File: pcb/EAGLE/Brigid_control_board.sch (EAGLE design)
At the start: 33 parts, among them J1 ARDUINO_R3_SHIELD, P1 Molex Mini-Fit Jr., P2 Molex Mini-Fit Jr., P3 Molex Mini-Fit Jr., P4 Molex Mini-Fit Jr., P5 Molex Mini-Fit Jr., P6 Molex Mini-Fit Jr., P7 Molex Mini-Fit Jr., Q1 T460, Q2 T460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

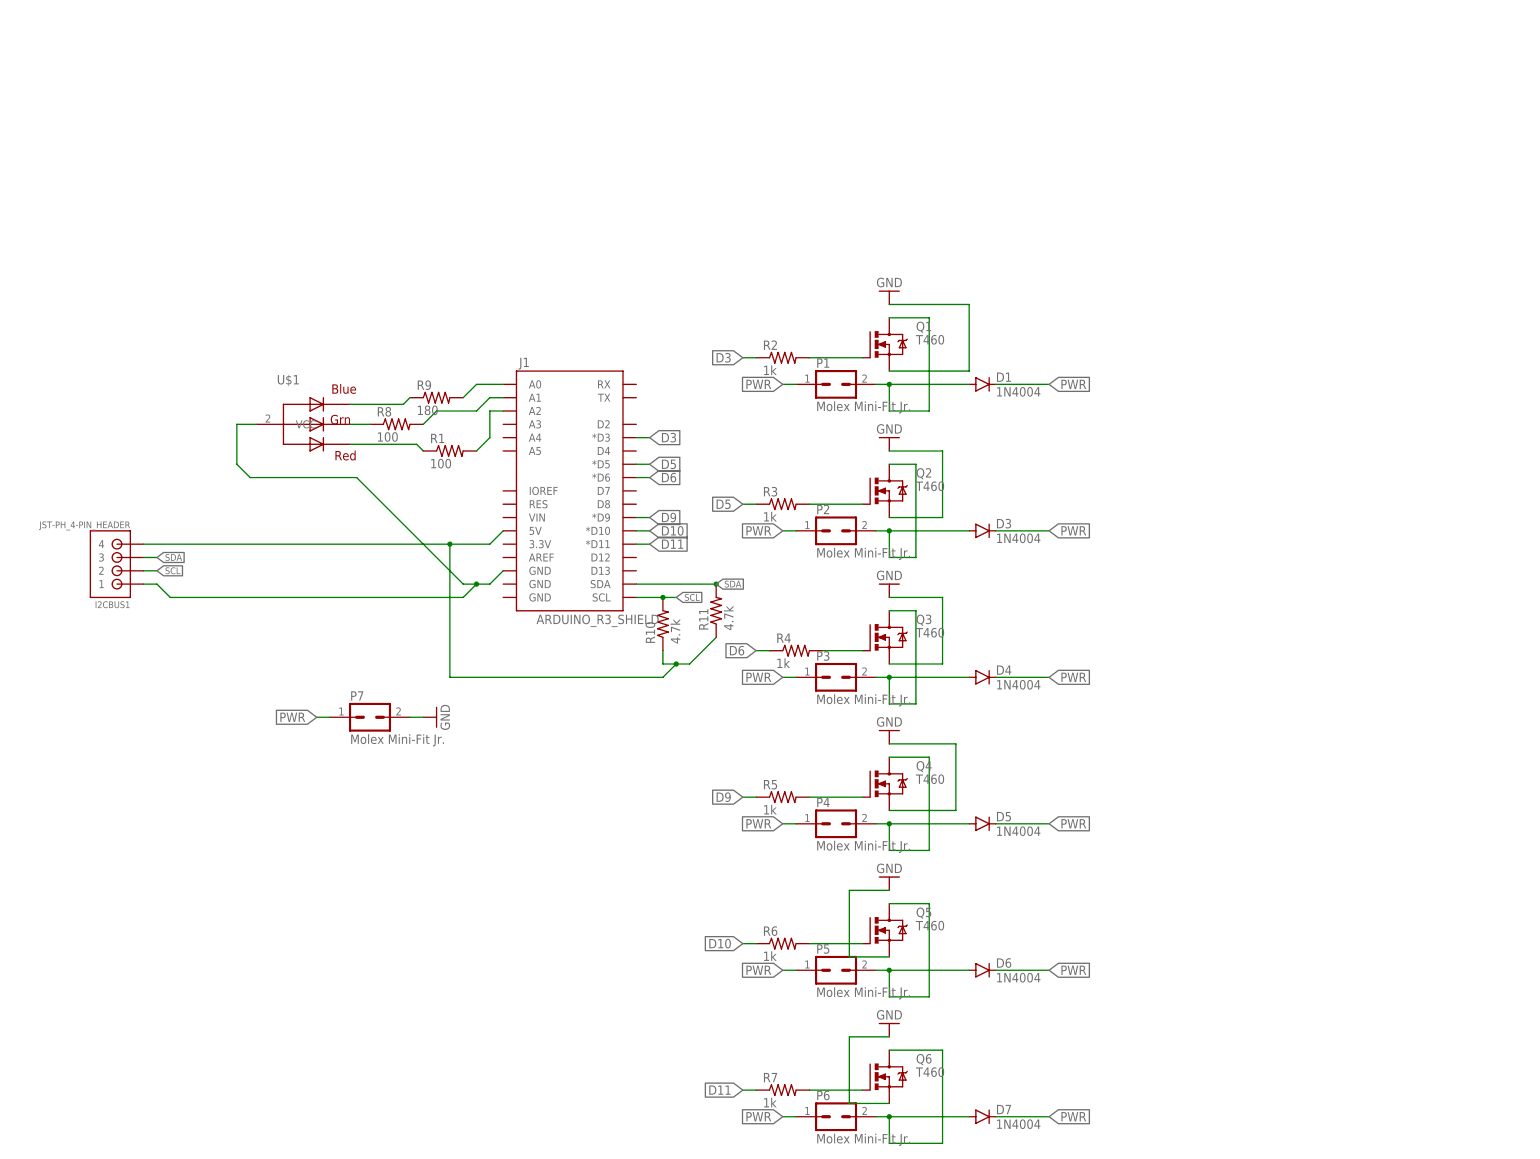
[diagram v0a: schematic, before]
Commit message: added firmware for DC_Motors
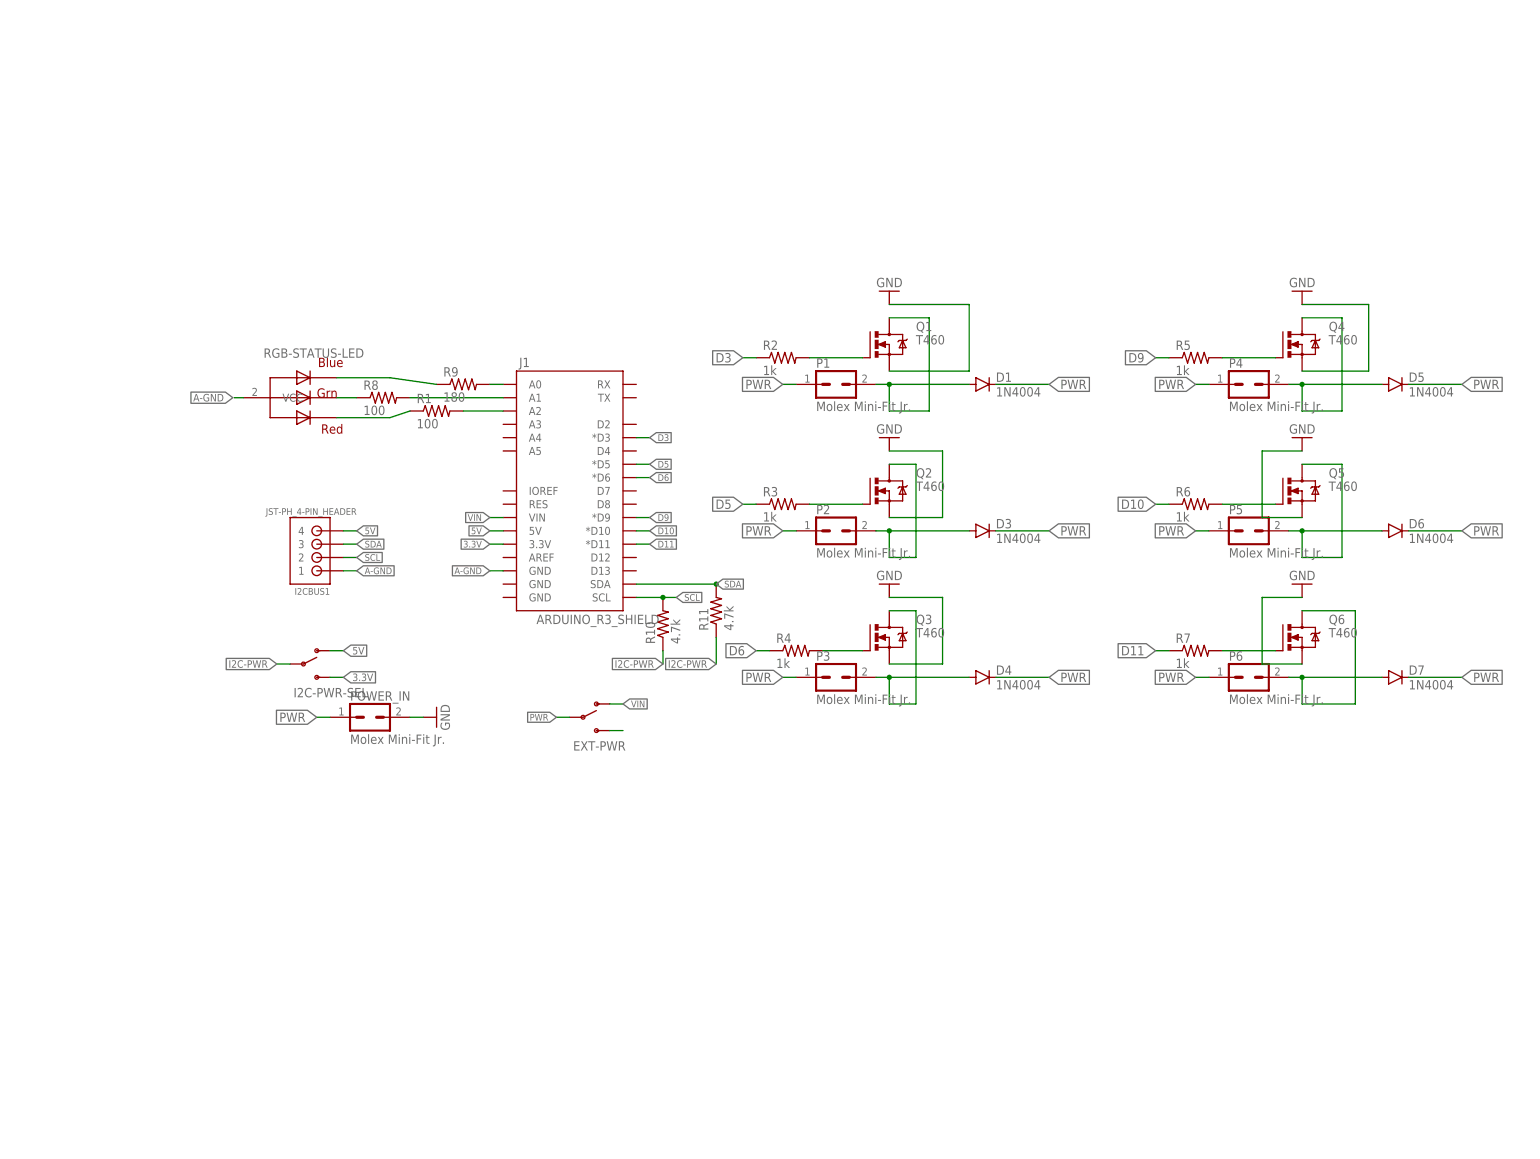
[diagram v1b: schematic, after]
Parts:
- removed U$1: RGB LED, adafruit:RGBLED_CA
- added EXT-PWR, I2C-PWR-SEL: (no value), SparkFun-Electromechanical:SWITCH-SPDTKIT
- added RGB-STATUS-LED: RGB LED, adafruit:RGBLED_CA
- renumbered P7 to POWER_IN
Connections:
- removed net N$20: I2CBUS1.1, J1.GND@2, U$1.VCC
- new net 3.3V: I2C-PWR-SEL.S, J1.3.3V
- new net 5V: I2C-PWR-SEL.O, I2CBUS1.4, J1.5V
- new net A-GND: I2CBUS1.1, J1.GND@2, RGB-STATUS-LED.VCC
- new net I2C-PWR: I2C-PWR-SEL.P, R10.1, R11.1
- new net VIN: EXT-PWR.O, J1.VIN
- net N$17: now also EXT-PWR.S; no longer I2CBUS1.4, J1.5V, R10.1, R11.1
- net N$5: now also RGB-STATUS-LED.BLUE; no longer U$1.BLUE
- net N$7: now also RGB-STATUS-LED.RED; no longer U$1.RED
- net N$8: now also RGB-STATUS-LED.GREEN; no longer U$1.GREEN
- net PWR: now also EXT-PWR.P
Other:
- moved on the sheet: D5, D6, D7, I2CBUS1, P4, P5, P6, Q4, Q5, Q6, R1, R5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

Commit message: updated brigid board, removed switched that were not needed
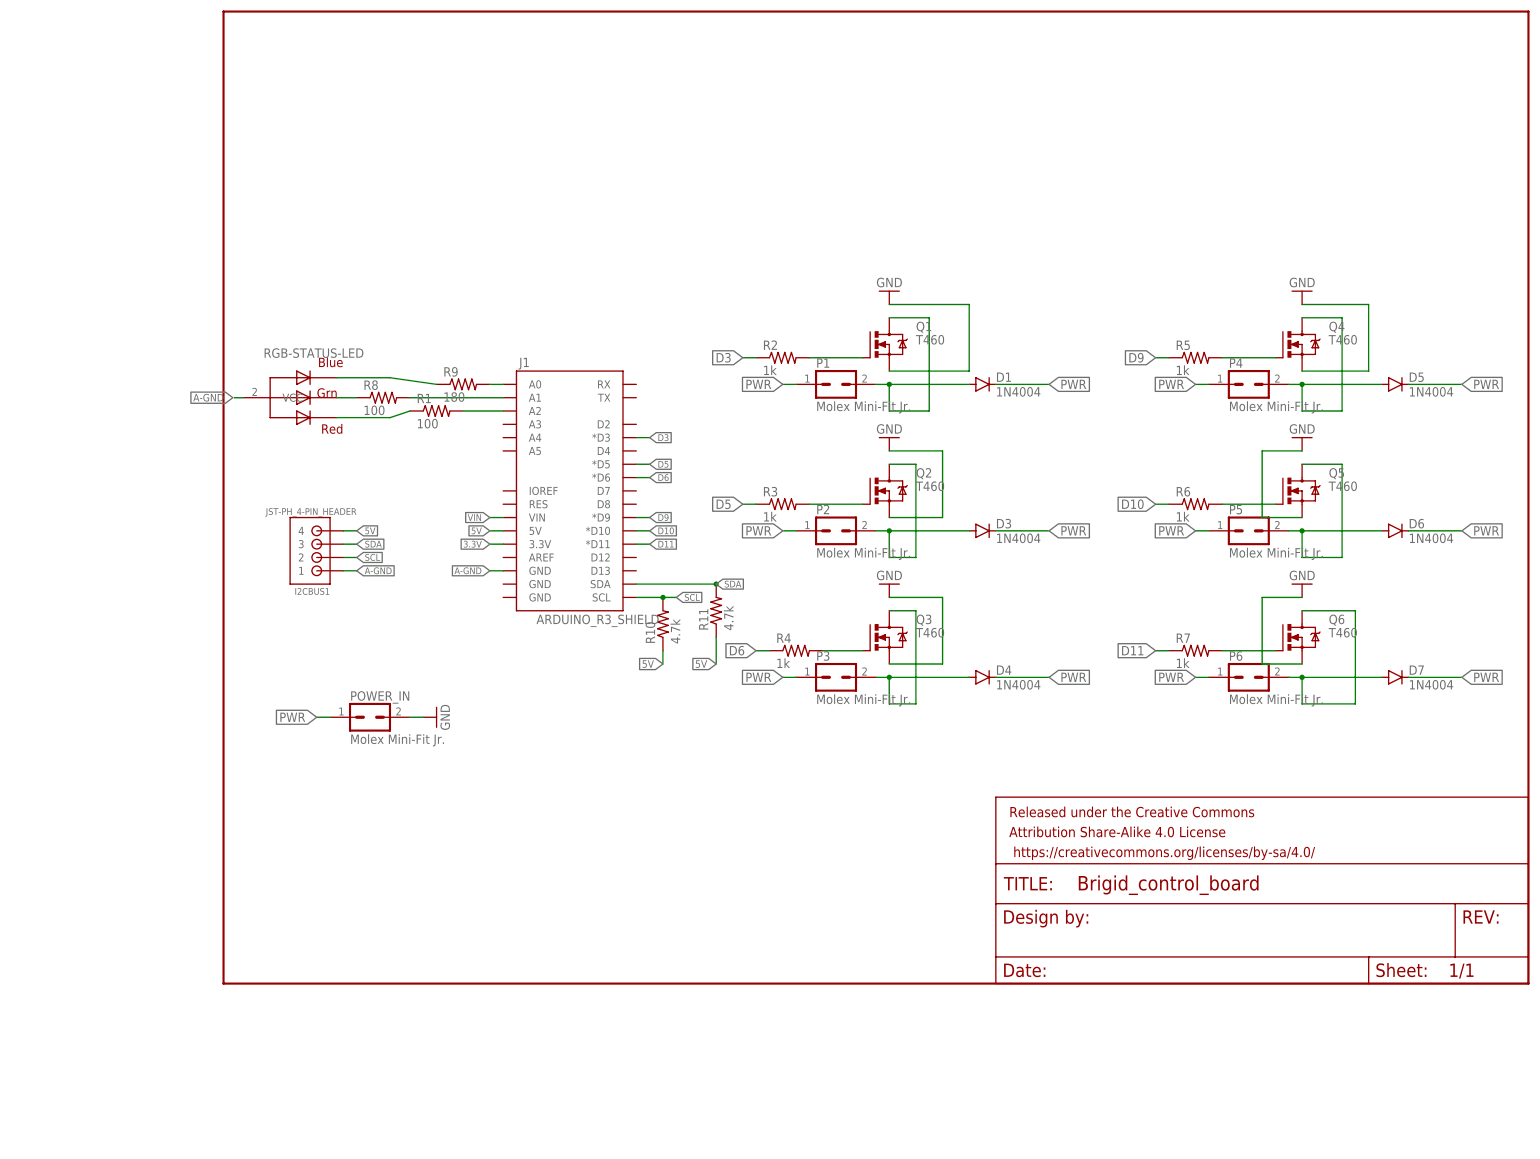
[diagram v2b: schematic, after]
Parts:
- removed EXT-PWR, I2C-PWR-SEL: (no value), SparkFun-Electromechanical:SWITCH-SPDTKIT
- added FRAME1: FRAME-LETTER, SparkFun-Aesthetics:FRAME-LETTER
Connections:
- removed net I2C-PWR: I2C-PWR-SEL.P, R10.1, R11.1
- removed net N$17: EXT-PWR.S
- net 3.3V: no longer I2C-PWR-SEL.S
- net 5V: now also R10.1, R11.1; no longer I2C-PWR-SEL.O
- net PWR: no longer EXT-PWR.P
- net VIN: no longer EXT-PWR.O
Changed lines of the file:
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@@
 <setting verticaltext="up"/>
 </settings>
-<grid distance="0.1" unitdist="inch" unit="inch" style="lines" multiple="1" display="yes" altdistance="0.01" altunitdist="inch" altunit="inch"/>
+<grid distance="0.1" unitdist="inch" unit="inch" style="lines" multiple="1" display="no" altdistance="0.01" altunitdist="inch" altunit="inch"/>
 <layers>
 <layer number="1" name="Top" color="4" fill="1" visible="no" active="no"/>
@@
 <part name="R10" library="SparkFun-Passives" deviceset="RESISTOR" device="EZ" value="4.7k"/>
 <part name="R11" library="SparkFun-Passives" deviceset="RESISTOR" device="EZ" value="4.7k"/>
-<part name="I2C-PWR-SEL" library="SparkFun-Electromechanical" deviceset="SWITCH-SPDT" device="KIT"/>
-<part name="EXT-PWR" library="SparkFun-Electromechanical" deviceset="SWITCH-SPDT" device="KIT"/>
+<part name="FRAME1" library="SparkFun-Aesthetics" deviceset="FRAME-LETTER" device=""/>
 </parts>
 <sheets>
@@
 <instance part="R10" gate="G$1" x="66.04" y="25.4" rot="R90"/>
 <instance part="R11" gate="G$1" x="76.2" y="27.94" rot="R90"/>
-<instance part="I2C-PWR-SEL" gate="1" x="-2.54" y="17.78"/>
-<instance part="EXT-PWR" gate="1" x="50.8" y="7.62"/>
+<instance part="FRAME1" gate="G$1" x="-17.78" y="-43.18"/>
+<instance part="FRAME1" gate="V" x="129.54" y="-43.18"/>
 </instances>
 <busses>
@@
 <label x="0" y="7.62" size="1.778" layer="95" rot="R180" xref="yes"/>
 </segment>
-<segment>
-<pinref part="EXT-PWR" gate="1" pin="P"/>
-<wire x1="48.26" y1="7.62" x2="45.72" y2="7.62" width="0.1524" layer="91"/>
-<label x="45.72" y="7.62" size="1.27" layer="95" rot="R180" xref="yes"/>
-</segment>
 </net>
 <net name="D3" class="0">
@@
 </segment>
 </net>
-<net name="I2C-PWR" class="0">
+<net name="A-GND" class="0">
+<segment>
+<pinref part="RGB-STATUS-LED" gate="G$1" pin="VCC"/>
+<wire x1="-13.97" y1="68.58" x2="-15.748" y2="68.58" width="0.1524" layer="91"/>
+<label x="-16.002" y="68.58" size="1.4224" layer="95" rot="R180" xref="yes"/>
+</segment>
+<segment>
+<pinref part="J1" gate="G$1" pin="GND@2"/>
+<wire x1="35.56" y1="35.56" x2="33.02" y2="35.56" width="0.1524" layer="91"/>
+<label x="33.02" y="35.56" size="1.27" layer="95" rot="R180" xref="yes"/>
+</segment>
+<segment>
+<pinref part="I2CBUS1" gate="G$1" pin="1"/>
+<wire x1="5.08" y1="35.56" x2="7.62" y2="35.56" width="0.1524" layer="91"/>
+<label x="7.62" y="35.56" size="1.27" layer="95" xref="yes"/>
+</segment>
+</net>
+<net name="5V" class="0">
+<segment>
+<pinref part="I2CBUS1" gate="G$1" pin="4"/>
+<wire x1="5.08" y1="43.18" x2="7.62" y2="43.18" width="0.127" layer="91"/>
+<label x="7.62" y="43.18" size="1.27" layer="95" xref="yes"/>
+</segment>
+<segment>
+<pinref part="J1" gate="G$1" pin="5V"/>
+<wire x1="35.56" y1="43.18" x2="33.02" y2="43.18" width="0.1524" layer="91"/>
+<label x="33.02" y="43.18" size="1.27" layer="95" rot="R180" xref="yes"/>
+</segment>
 <segment>
 <pinref part="R10" gate="G$1" pin="1"/>
@@
 <label x="76.2" y="17.78" size="1.4224" layer="95" rot="R180" xref="yes"/>
 </segment>
-<segment>
-<pinref part="I2C-PWR-SEL" gate="1" pin="P"/>
-<wire x1="-5.08" y1="17.78" x2="-7.62" y2="17.78" width="0.1524" layer="91"/>
-<label x="-7.62" y="17.78" size="1.4224" layer="95" rot="R180" xref="yes"/>
-</segment>
-</net>
-<net name="A-GND" class="0">
-<segment>
-<pinref part="RGB-STATUS-LED" gate="G$1" pin="VCC"/>
-<wire x1="-13.97" y1="68.58" x2="-15.748" y2="68.58" width="0.1524" layer="91"/>
-<label x="-16.002" y="68.58" size="1.4224" layer="95" rot="R180" xref="yes"/>
-</segment>
-<segment>
-<pinref part="J1" gate="G$1" pin="GND@2"/>
-<wire x1="35.56" y1="35.56" x2="33.02" y2="35.56" width="0.1524" layer="91"/>
-<label x="33.02" y="35.56" size="1.27" layer="95" rot="R180" xref="yes"/>
-</segment>
-<segment>
-<pinref part="I2CBUS1" gate="G$1" pin="1"/>
-<wire x1="5.08" y1="35.56" x2="7.62" y2="35.56" width="0.1524" layer="91"/>
-<label x="7.62" y="35.56" size="1.27" layer="95" xref="yes"/>
-</segment>
-</net>
-<net name="5V" class="0">
-<segment>
-<pinref part="I2CBUS1" gate="G$1" pin="4"/>
-<wire x1="5.08" y1="43.18" x2="7.62" y2="43.18" width="0.127" layer="91"/>
-<label x="7.62" y="43.18" size="1.27" layer="95" xref="yes"/>
-</segment>
-<segment>
-<pinref part="J1" gate="G$1" pin="5V"/>
-<wire x1="35.56" y1="43.18" x2="33.02" y2="43.18" width="0.1524" layer="91"/>
-<label x="33.02" y="43.18" size="1.27" layer="95" rot="R180" xref="yes"/>
-</segment>
-<segment>
-<pinref part="I2C-PWR-SEL" gate="1" pin="O"/>
-<wire x1="2.54" y1="20.32" x2="5.08" y2="20.32" width="0.1524" layer="91"/>
-<label x="5.08" y="20.32" size="1.4224" layer="95" xref="yes"/>
-</segment>
 </net>
 <net name="3.3V" class="0">
-<segment>
-<pinref part="I2C-PWR-SEL" gate="1" pin="S"/>
-<wire x1="2.54" y1="15.24" x2="5.08" y2="15.24" width="0.1524" layer="91"/>
-<label x="5.08" y="15.24" size="1.4224" layer="95" xref="yes"/>
-</segment>
 <segment>
 <pinref part="J1" gate="G$1" pin="3.3V"/>
@@
 <net name="VIN" class="0">
 <segment>
-<pinref part="EXT-PWR" gate="1" pin="O"/>
-<wire x1="55.88" y1="10.16" x2="58.42" y2="10.16" width="0.1524" layer="91"/>
-<label x="58.42" y="10.16" size="1.27" layer="95" xref="yes"/>
-</segment>
-<segment>
 <pinref part="J1" gate="G$1" pin="VIN"/>
 <wire x1="35.56" y1="45.72" x2="33.02" y2="45.72" width="0.1524" layer="91"/>
@@
 </segment>
 </net>
-<net name="N$17" class="0">
-<segment>
-<pinref part="EXT-PWR" gate="1" pin="S"/>
-<wire x1="55.88" y1="5.08" x2="58.42" y2="5.08" width="0.1524" layer="91"/>
-</segment>
-</net>
